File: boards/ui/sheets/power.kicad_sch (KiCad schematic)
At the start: 26 parts, among them J6 Barrel_Jack_Switch, J8 TB001-500-02BE, U2 TL072

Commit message: Added FAB drawings of all boards for UI
As a preparation for making everything more streamlined
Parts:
- removed J8: TB001-500-02BE, Shmoergh_Custom_Footprints:CUI_TB001-500-02BE, symbol Shmoergh-Custom-Components:TB001-500-02BE
- added J9: Conn_02x04_Odd_Even, Connector_PinHeader_2.54mm:PinHeader_2x04_P2.54mm_Vertical, symbol Connector_Generic:Conn_02x04_Odd_Even
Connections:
- net 12VDC_SW_NEG: now also J9.5 (Pin_5), J9.6 (Pin_6), J9.7 (Pin_7), J9.8 (Pin_8)
- net 12VDC_SW_POS: now also J9.1 (Pin_1), J9.2 (Pin_2), J9.3 (Pin_3), J9.4 (Pin_4)

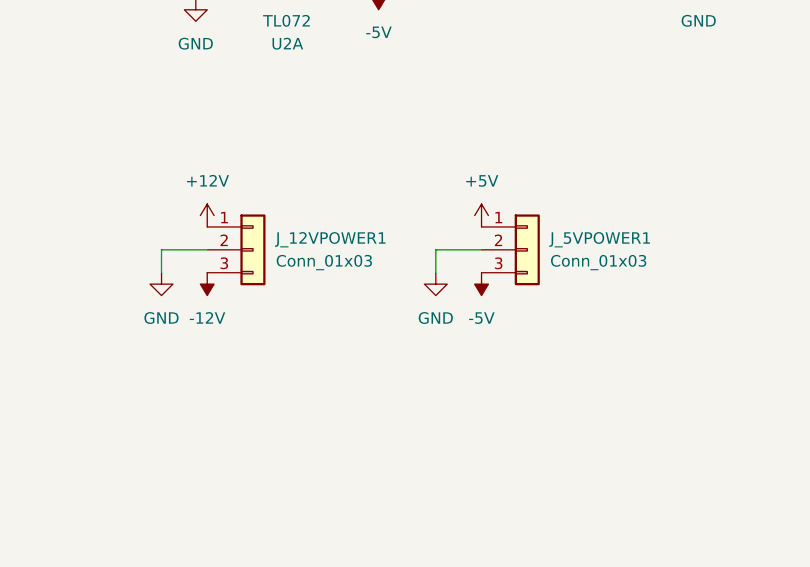
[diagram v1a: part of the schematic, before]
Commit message: Added production files for the UI board
ref https://github.com/shmoergh/hog/issues/19
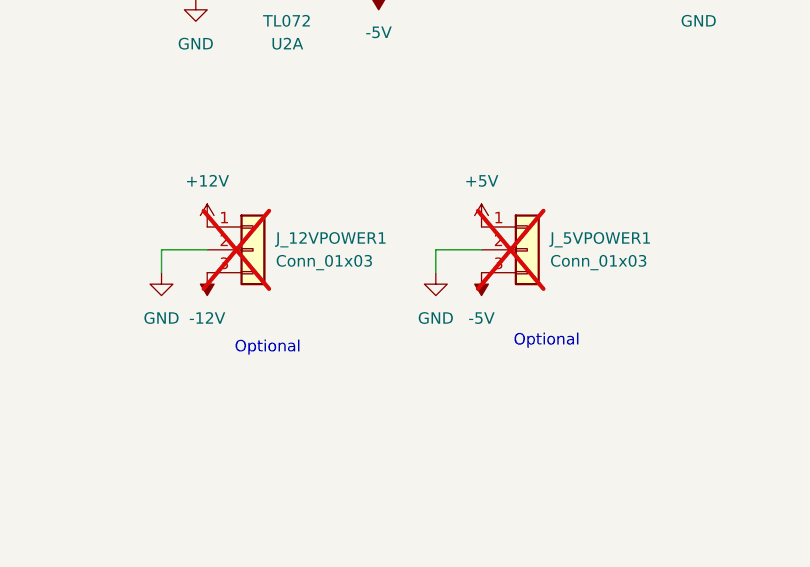
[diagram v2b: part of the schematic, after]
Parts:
- C201, C202: Part No. (none) -> 80-ESS107M025AE2AA; Part URL (none) -> https://mou.sr/3ZTs1yq; Vendor (none) -> Mouser; now in the parts list
- C201: Part No. (none) -> 667-ECE-A1VKS470I; Part URL (none) -> https://mou.sr/4iyQHDI; Vendor (none) -> Mouser; now in the parts list
- C202: Part No. (none) -> 667-ECE-A1VKS470I; Part URL (none) -> https://mou.sr/4iyQHDI; Vendor (none) -> Mouser
- C3: Part No. (none) -> 594-K103K15X7RF5TK2; Part URL (none) -> https://mou.sr/3VFZIRH; Vendor (none) -> Mouser
- J6: Part No. (none) -> 710-694106301002; Part URL (none) -> https://mou.sr/4a9ckVQ; Vendor (none) -> Mouser
- J9: Part No. (none) -> 737-PH2-08-UA; Part URL (none) -> https://mou.sr/4gxLnib; Vendor (none) -> Mouser
- J_12VPOWER1, J_5VPOWER1: now not fitted; now left out of the parts list
- J_CORE_POWER1: Part No. (none) -> 737-PH2-10-UA; Part URL (none) -> https://mou.sr/3D13TAT; Vendor (none) -> Mouser; now in the parts list
- R17: Part No. (none) -> 303-CFR0W4J0202B00; Part URL (none) -> https://mou.sr/3BpNNAx; Vendor (none) -> Mouser
- R21, R25: Part No. (none) -> 303-MF0W4FF1002T50; Part URL (none) -> https://mou.sr/3VFoGR5; Vendor (none) -> Mouser
- RV_MAIN_VCO_5V1: Part No. (none) -> 652-3006P-1-103-LF; Part URL (none) -> https://mou.sr/41xh2vW; Vendor (none) -> Mouser
- S1: Mouser https://mou.sr/3TDv9tV -> (none); Part No. (none) -> 612-PB400EEQR1BLK; Part URL (none) -> https://mou.sr/3TDv9tV; Vendor (none) -> Mouser
- TP_-5V1, TP_5V1: now left out of the parts list
- U2: Part No. (none) -> 595-TL072IP; Part URL (none) -> https://mou.sr/4g5XjI5; Vendor (none) -> Mouser
- U_5VREF1: footprint Package_TO_SOT_THT:TO-92L_Inline -> Package_TO_SOT_THT:TO-92L_Inline_Wide; Mouser https://hu.mouser.com/ProductDetail/Texas-Instruments/LM336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 -> (none); Part No. (none) -> 926-LM336Z-50/NOPB; Part URL (none) -> https://mou.sr/3y3TEcP; Vendor (none) -> Mouser
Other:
- note added: "Optional"

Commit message: Updated resistor Mouser no's and added full bom
- Some of the THT resistors in the BOM were referencing to products with min. 1000 pcs order quantity
- Added a full Mouser BOM which can be used to order all Mouser components by uploading to their BOM tool: https://hu.mouser.com/bom/
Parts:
- R17: Part No. 303-CFR0W4J0202B00 -> 603-MFR-25FTF52-2K; Part URL https://mou.sr/3BpNNAx -> https://mou.sr/425kXjj
- R21, R25: Part No. 303-MF0W4FF1002T50 -> 603-MFR25SFRF52-10K; Part URL https://mou.sr/3VFoGR5 -> https://mou.sr/3XU3MyE
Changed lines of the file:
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@@
 	(label "12VDC_WALLWART"
 		(at 90.17 34.29 90)
-		(fields_autoplaced yes)
 		(effects
 			(font
@@
 	(label "12VDC_SW_NEG"
 		(at 111.76 54.61 180)
-		(fields_autoplaced yes)
 		(effects
 			(font
@@
 	(label "12VDC_SW_POS"
 		(at 116.84 34.29 90)
-		(fields_autoplaced yes)
 		(effects
 			(font
@@
 			)
 		)
-		(property "Part No." "303-MF0W4FF1002T50 "
+		(property "Part No." "603-MFR25SFRF52-10K "
 			(at 190.5 87.63 0)
 			(effects
@@
 			)
 		)
-		(property "Part URL" "https://mou.sr/3VFoGR5"
+		(property "Part URL" "https://mou.sr/3XU3MyE"
 			(at 190.5 87.63 0)
 			(effects
@@
 			)
 		)
-		(property "Part No." "303-MF0W4FF1002T50 "
+		(property "Part No." "603-MFR25SFRF52-10K "
 			(at 171.45 96.52 0)
 			(effects
@@
 			)
 		)
-		(property "Part URL" "https://mou.sr/3VFoGR5"
+		(property "Part URL" "https://mou.sr/3XU3MyE"
 			(at 171.45 96.52 0)
 			(effects
@@
 			)
 		)
-		(property "Part No." "303-CFR0W4J0202B00 "
+		(property "Part No." "603-MFR-25FTF52-2K"
 			(at 116.84 77.47 0)
 			(effects
@@
 			)
 		)
-		(property "Part URL" "https://mou.sr/3BpNNAx"
+		(property "Part URL" "https://mou.sr/425kXjj"
 			(at 116.84 77.47 0)
 			(effects
